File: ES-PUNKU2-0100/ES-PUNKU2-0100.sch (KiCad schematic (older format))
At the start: 0 parts

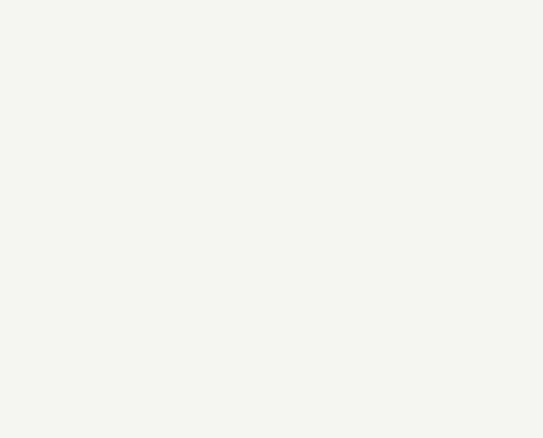
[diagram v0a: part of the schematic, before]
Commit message: Incorporación de las correcciones sugeridas por Martin Ribelotta y posicionamiento de componentes
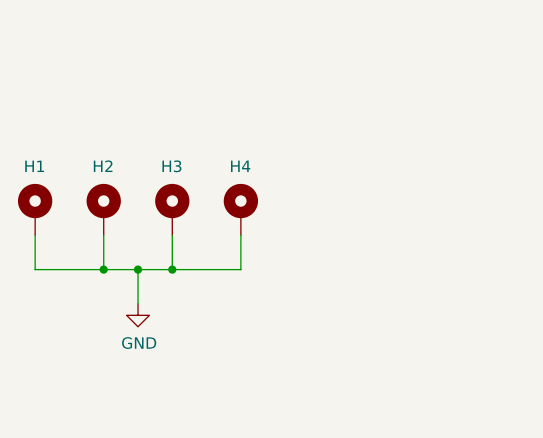
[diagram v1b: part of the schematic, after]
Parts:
- added H1, H2, H3, H4: MountingHole_Pad, MountingHole:MountingHole_4mm_Pad, symbol Mechanical:MountingHole_Pad
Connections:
- new net GND: H1.1, H2.1, H3.1, H4.1
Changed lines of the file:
@@
 Title "PUNKU"
 Date "2019-09-09"
-Rev "1.00"
+Rev "1.01"
 Comp "EQUISER"
-Comment1 "E.Volentini (2019-09-09)"
-Comment2 ""
-Comment3 ""
+Comment1 "Esteban Volentini (2019-09-09)"
+Comment2 "Agustin Rey (2019-09-25)"
+Comment3 "Martin Ribelotta  (2019-09-27)"
 Comment4 ""
 $EndDescr
@@
 Wire Wire Line
 	5400 4200 6000 4200
+$Comp
+L Mechanical:MountingHole_Pad H1
+U 1 1 5D97B5E5
+P 2050 3550
+F 0 "H1" H 2000 3750 50  0000 L CNN
+F 1 "MountingHole_Pad" H 2150 3508 50  0001 L CNN
+F 2 "MountingHole:MountingHole_4mm_Pad" H 2050 3550 50  0001 C CNN
+F 3 "~" H 2050 3550 50  0001 C CNN
+	1    2050 3550
+	1    0    0    -1
+$EndComp
+$Comp
+L Mechanical:MountingHole_Pad H2
+U 1 1 5D97C991
+P 2350 3550
+F 0 "H2" H 2300 3750 50  0000 L CNN
+F 1 "MountingHole_Pad" H 2450 3508 50  0001 L CNN
+F 2 "MountingHole:MountingHole_4mm_Pad" H 2350 3550 50  0001 C CNN
+F 3 "~" H 2350 3550 50  0001 C CNN
+	1    2350 3550
+	1    0    0    -1
+$EndComp
+$Comp
+L Mechanical:MountingHole_Pad H3
+U 1 1 5D97CF02
+P 2650 3550
+F 0 "H3" H 2600 3750 50  0000 L CNN
+F 1 "MountingHole_Pad" H 2750 3508 50  0001 L CNN
+F 2 "MountingHole:MountingHole_4mm_Pad" H 2650 3550 50  0001 C CNN
+F 3 "~" H 2650 3550 50  0001 C CNN
+	1    2650 3550
+	1    0    0    -1
+$EndComp
+$Comp
+L Mechanical:MountingHole_Pad H4
+U 1 1 5D97D2BE
+P 2950 3550
+F 0 "H4" H 2900 3750 50  0000 L CNN
+F 1 "MountingHole_Pad" H 3050 3508 50  0001 L CNN
+F 2 "MountingHole:MountingHole_4mm_Pad" H 2950 3550 50  0001 C CNN
+F 3 "~" H 2950 3550 50  0001 C CNN
+	1    2950 3550
+	1    0    0    -1
+$EndComp
+Wire Wire Line
+	2050 3650 2050 3800
+Wire Wire Line
+	2050 3800 2350 3800
+Wire Wire Line
+	2950 3800 2950 3650
+Wire Wire Line
+	2350 3650 2350 3800
+Connection ~ 2350 3800
+Wire Wire Line
+	2350 3800 2500 3800
+Wire Wire Line
+	2650 3650 2650 3800
+Connection ~ 2650 3800
+Wire Wire Line
+	2650 3800 2950 3800
+$Comp
+L power:GND #PWR01
+U 1 1 5D97DCD0
+P 2500 3950
+F 0 "#PWR01" H 2500 3700 50  0001 C CNN
+F 1 "GND" H 2505 3777 50  0000 C CNN
+F 2 "" H 2500 3950 50  0001 C CNN
+F 3 "" H 2500 3950 50  0001 C CNN
+	1    2500 3950
+	1    0    0    -1
+$EndComp
+Wire Wire Line
+	2500 3950 2500 3800
+Connection ~ 2500 3800
+Wire Wire Line
+	2500 3800 2650 3800
 $EndSCHEMATC

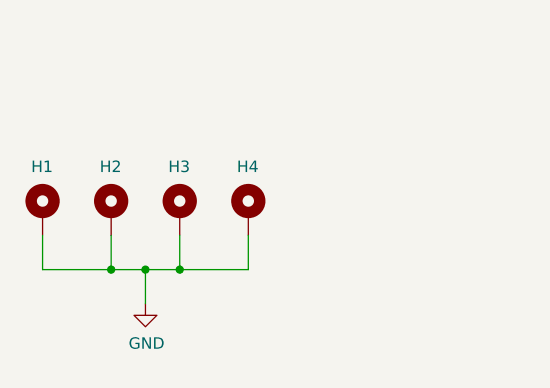
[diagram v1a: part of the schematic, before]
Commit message: Correcciónes y exportacion del modelo 3D de la placa
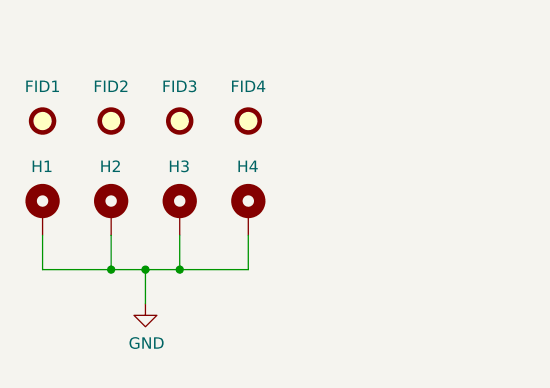
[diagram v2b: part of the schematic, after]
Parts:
- added FID1, FID2, FID3, FID4: Fiducial, Fiducial:Fiducial_0.5mm_Mask1mm, symbol Mechanical:Fiducial
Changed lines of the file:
@@
 Wire Wire Line
 	2500 3800 2650 3800
+$Comp
+L Mechanical:Fiducial FID1
+U 1 1 5DA52320
+P 2050 3150
+F 0 "FID1" H 2050 3300 50  0000 C CNN
+F 1 "Fiducial" H 2135 3105 50  0001 L CNN
+F 2 "Fiducial:Fiducial_0.5mm_Mask1mm" H 2050 3150 50  0001 C CNN
+F 3 "~" H 2050 3150 50  0001 C CNN
+	1    2050 3150
+	1    0    0    -1
+$EndComp
+$Comp
+L Mechanical:Fiducial FID2
+U 1 1 5DA52F42
+P 2350 3150
+F 0 "FID2" H 2350 3300 50  0000 C CNN
+F 1 "Fiducial" H 2435 3105 50  0001 L CNN
+F 2 "Fiducial:Fiducial_0.5mm_Mask1mm" H 2350 3150 50  0001 C CNN
+F 3 "~" H 2350 3150 50  0001 C CNN
+	1    2350 3150
+	1    0    0    -1
+$EndComp
+$Comp
+L Mechanical:Fiducial FID3
+U 1 1 5DA53223
+P 2650 3150
+F 0 "FID3" H 2650 3300 50  0000 C CNN
+F 1 "Fiducial" H 2735 3105 50  0001 L CNN
+F 2 "Fiducial:Fiducial_0.5mm_Mask1mm" H 2650 3150 50  0001 C CNN
+F 3 "~" H 2650 3150 50  0001 C CNN
+	1    2650 3150
+	1    0    0    -1
+$EndComp
+$Comp
+L Mechanical:Fiducial FID4
+U 1 1 5DA5335B
+P 2950 3150
+F 0 "FID4" H 2950 3300 50  0000 C CNN
+F 1 "Fiducial" H 3035 3105 50  0001 L CNN
+F 2 "Fiducial:Fiducial_0.5mm_Mask1mm" H 2950 3150 50  0001 C CNN
+F 3 "~" H 2950 3150 50  0001 C CNN
+	1    2950 3150
+	1    0    0    -1
+$EndComp
 $EndSCHEMATC

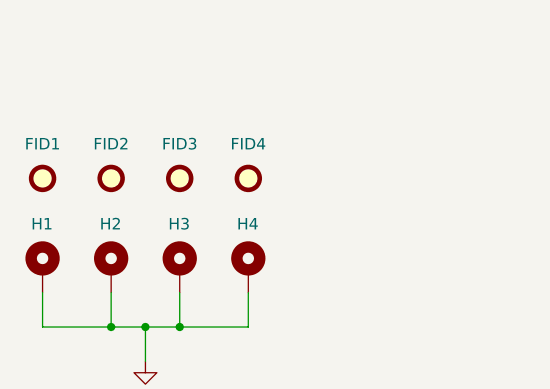
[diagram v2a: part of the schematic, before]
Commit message: Correcciones de ruteo y agregado de una protección para la salida del puente H
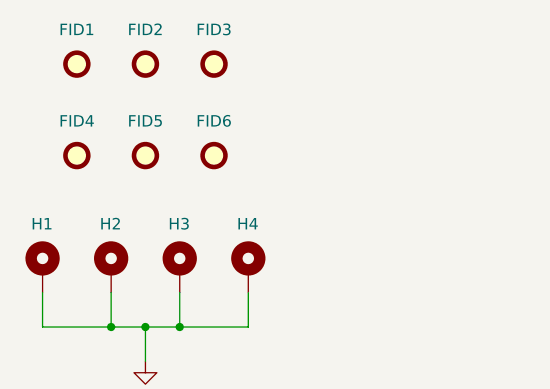
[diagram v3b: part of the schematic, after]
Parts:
- added FID5, FID6: Fiducial, Fiducial:Fiducial_0.5mm_Mask1mm, symbol Mechanical:Fiducial
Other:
- moved on the sheet: FID1, FID2, FID3, FID4
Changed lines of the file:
@@
 Sheet 1 3
 Title "PUNKU"
-Date "2019-09-09"
-Rev "1.01"
+Date "2019-10-18"
+Rev "1.02"
 Comp "EQUISER"
-Comment1 "Esteban Volentini (2019-09-09)"
+Comment1 "Esteban Volentini (2019-10-18)"
 Comment2 "Agustin Rey (2019-09-25)"
 Comment3 "Martin Ribelotta  (2019-09-27)"
@@
 L Mechanical:Fiducial FID1
 U 1 1 5DA52320
-P 2050 3150
-F 0 "FID1" H 2050 3300 50  0000 C CNN
-F 1 "Fiducial" H 2135 3105 50  0001 L CNN
-F 2 "Fiducial:Fiducial_0.5mm_Mask1mm" H 2050 3150 50  0001 C CNN
-F 3 "~" H 2050 3150 50  0001 C CNN
-	1    2050 3150
+P 2200 2650
+F 0 "FID1" H 2200 2800 50  0000 C CNN
+F 1 "Fiducial" H 2285 2605 50  0001 L CNN
+F 2 "Fiducial:Fiducial_0.5mm_Mask1mm" H 2200 2650 50  0001 C CNN
+F 3 "~" H 2200 2650 50  0001 C CNN
+	1    2200 2650
 	1    0    0    -1
 $EndComp
@@
 L Mechanical:Fiducial FID2
 U 1 1 5DA52F42
-P 2350 3150
-F 0 "FID2" H 2350 3300 50  0000 C CNN
-F 1 "Fiducial" H 2435 3105 50  0001 L CNN
-F 2 "Fiducial:Fiducial_0.5mm_Mask1mm" H 2350 3150 50  0001 C CNN
-F 3 "~" H 2350 3150 50  0001 C CNN
-	1    2350 3150
+P 2500 2650
+F 0 "FID2" H 2500 2800 50  0000 C CNN
+F 1 "Fiducial" H 2585 2605 50  0001 L CNN
+F 2 "Fiducial:Fiducial_0.5mm_Mask1mm" H 2500 2650 50  0001 C CNN
+F 3 "~" H 2500 2650 50  0001 C CNN
+	1    2500 2650
 	1    0    0    -1
 $EndComp
@@
 L Mechanical:Fiducial FID3
 U 1 1 5DA53223
-P 2650 3150
-F 0 "FID3" H 2650 3300 50  0000 C CNN
-F 1 "Fiducial" H 2735 3105 50  0001 L CNN
-F 2 "Fiducial:Fiducial_0.5mm_Mask1mm" H 2650 3150 50  0001 C CNN
-F 3 "~" H 2650 3150 50  0001 C CNN
-	1    2650 3150
+P 2800 2650
+F 0 "FID3" H 2800 2800 50  0000 C CNN
+F 1 "Fiducial" H 2885 2605 50  0001 L CNN
+F 2 "Fiducial:Fiducial_0.5mm_Mask1mm" H 2800 2650 50  0001 C CNN
+F 3 "~" H 2800 2650 50  0001 C CNN
+	1    2800 2650
 	1    0    0    -1
 $EndComp
@@
 L Mechanical:Fiducial FID4
 U 1 1 5DA5335B
-P 2950 3150
-F 0 "FID4" H 2950 3300 50  0000 C CNN
-F 1 "Fiducial" H 3035 3105 50  0001 L CNN
-F 2 "Fiducial:Fiducial_0.5mm_Mask1mm" H 2950 3150 50  0001 C CNN
-F 3 "~" H 2950 3150 50  0001 C CNN
-	1    2950 3150
-	1    0    0    -1
-$EndComp
+P 2200 3050
+F 0 "FID4" H 2200 3200 50  0000 C CNN
+F 1 "Fiducial" H 2285 3005 50  0001 L CNN
+F 2 "Fiducial:Fiducial_0.5mm_Mask1mm" H 2200 3050 50  0001 C CNN
+F 3 "~" H 2200 3050 50  0001 C CNN
+	1    2200 3050
+	1    0    0    -1
+$EndComp
+$Comp
+L Mechanical:Fiducial FID5
+U 1 1 5DAB5042
+P 2500 3050
+F 0 "FID5" H 2500 3200 50  0000 C CNN
+F 1 "Fiducial" H 2585 3005 50  0001 L CNN
+F 2 "Fiducial:Fiducial_0.5mm_Mask1mm" H 2500 3050 50  0001 C CNN
+F 3 "~" H 2500 3050 50  0001 C CNN
+	1    2500 3050
+	1    0    0    -1
+$EndComp
+$Comp
+L Mechanical:Fiducial FID6
+U 1 1 5DAB5587
+P 2800 3050
+F 0 "FID6" H 2800 3200 50  0000 C CNN
+F 1 "Fiducial" H 2885 3005 50  0001 L CNN
+F 2 "Fiducial:Fiducial_0.5mm_Mask1mm" H 2800 3050 50  0001 C CNN
+F 3 "~" H 2800 3050 50  0001 C CNN
+	1    2800 3050
+	1    0    0    -1
+$EndComp
